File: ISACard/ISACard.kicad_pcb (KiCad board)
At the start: 2 copper layers, 171.5 x 95.9 mm, 96 parts, among them J1 Bus_ISA_8bit, J2 ICSP, J3 EXTSPI, J4 SERCON, J5 Conn_01x16, Q1 2N3904, SW1 SW_Push, U1 74LS86, U10 28C256, U11 ATmega328P-P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

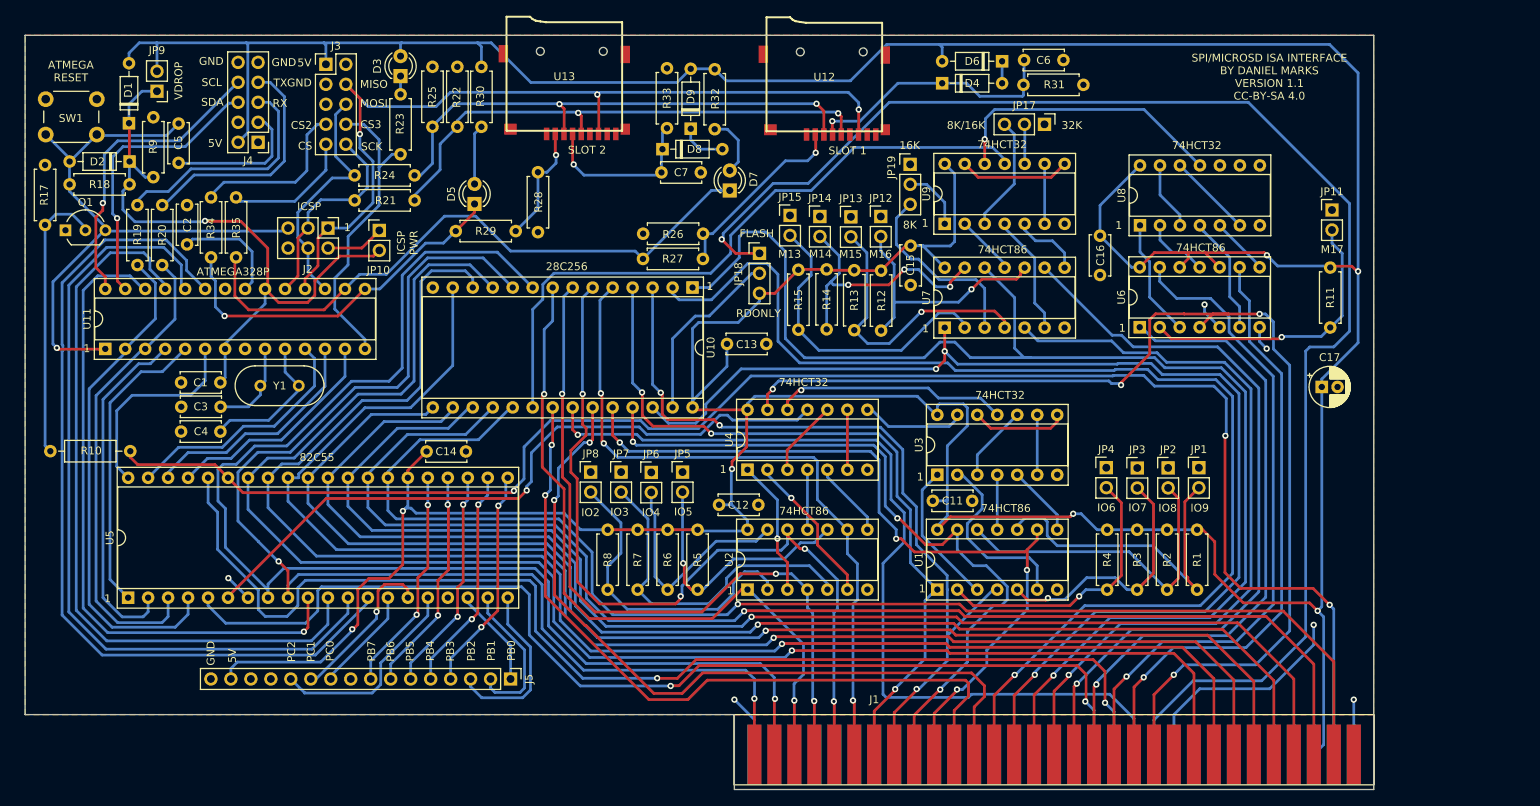
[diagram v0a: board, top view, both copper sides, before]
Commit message: moved SD card slots to edge
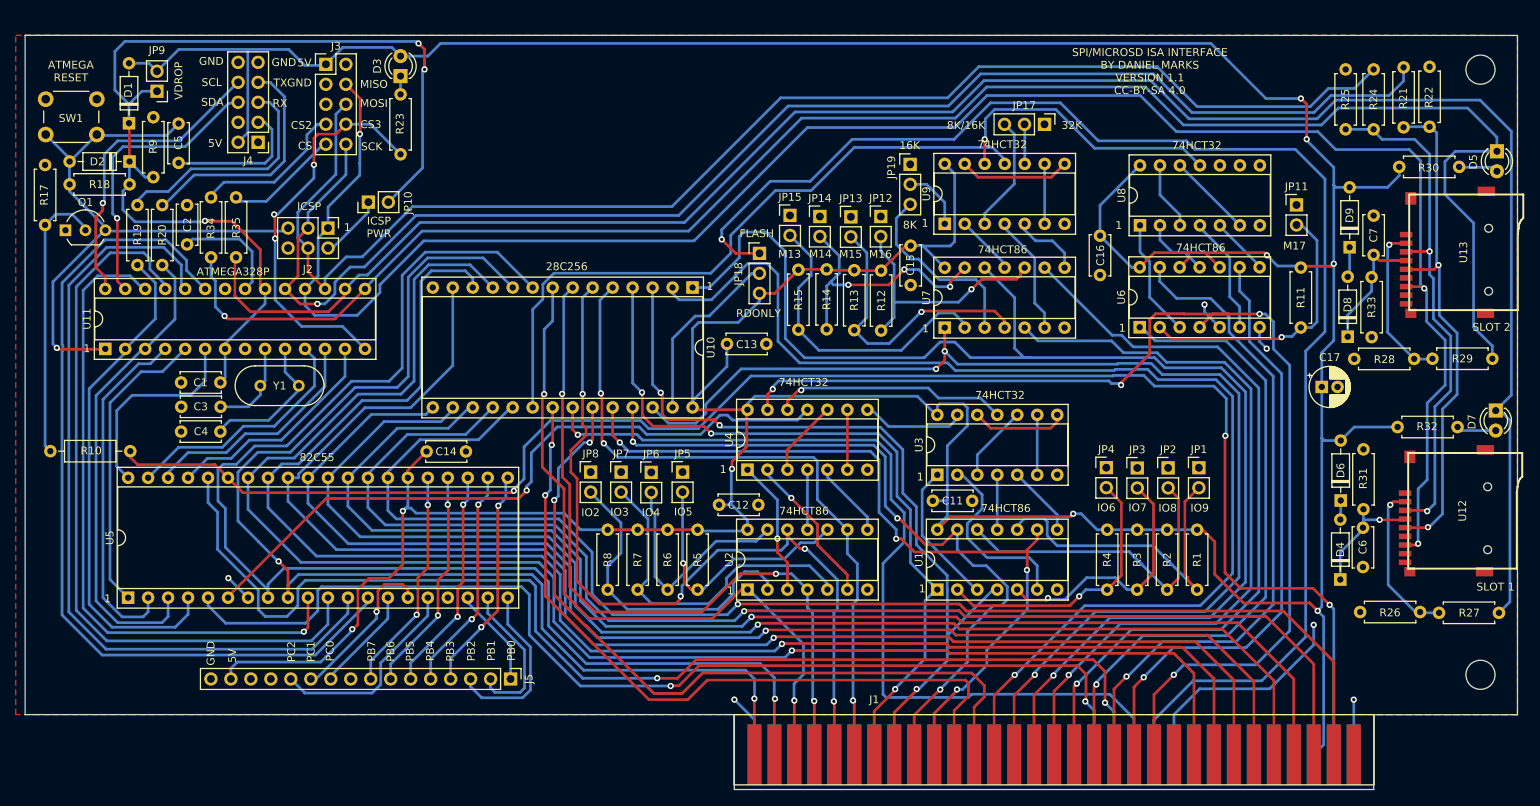
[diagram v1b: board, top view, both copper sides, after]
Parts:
- added H1: MountingHole, MountingHole:MountingHole_3.7mm, F.Cu at (236.0, 66.0)
- added H2: MountingHole, MountingHole:MountingHole_3.7mm, F.Cu at (236.0, 142.9)
- moved R21 134.4 mm to (226.2, 65.7), turned to -90 degrees
- moved R24 130.2 mm to (222.4, 66.0), turned to -90 degrees
- moved D5 130.1 mm to (238.1, 76.4), turned to -90 degrees
- moved R30 124.4 mm to (233.3, 78.4), turned to 180 degrees
- moved R22 123.6 mm to (229.5, 73.3)
- moved R29 117.7 mm to (229.9, 102.8), turned to 0 degrees
- moved R25 116.1 mm to (218.9, 73.6)
- moved R28 113.9 mm to (227.6, 102.8), turned to 180 degrees
- moved U13 107.2 mm to (225.7, 89.2), turned to -90 degrees
- moved R27 103.8 mm to (230.7, 135.1), turned to 0 degrees
- moved R26 103.1 mm to (228.3, 134.9)
- moved D7 101.3 mm to (237.9, 109.3), turned to -90 degrees
- moved R32 98.0 mm to (225.5, 111.4), turned to 0 degrees
- moved R33 91.6 mm to (222.2, 92.4), turned to -90 degrees
- moved D8 90.3 mm to (219.1, 100.0), turned to 90 degrees
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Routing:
- net CS2: track 46.5 -> 223.3 mm
- net CS: track 79.2 -> 248.8 mm
- net SCK: track 26.5 -> 183.0 mm, vias 0 -> 1
- net MOSI: track 30.5 -> 177.3 mm
- net MISO: track 109.8 -> 245.2 mm
- net Net-(D1-K): track 81.0 -> 130.2 mm, vias 1 -> 3
- net Net-(D4-K): track 33.3 -> 15.5 mm
- net CS3: track 39.0 -> 50.3 mm, vias 0 -> 3
- net +5V: track 631.5 -> 622.8 mm, vias 7 -> 9
- net Net-(D8-K): track 21.8 -> 16.2 mm, vias 1 -> 0
- net Net-(U13-~{CS}): track 15.2 -> 20.6 mm
- net Net-(U12-~{CS}): track 24.4 -> 20.3 mm
- net MEMW: track 185.5 -> 181.5 mm
- net Net-(D7-A): track 7.87 -> 5.04 mm
- net Net-(D5-A): track 7.63 -> 5.03 mm
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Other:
- board size 171.5 x 95.9 mm -> 189.7 x 95.9 mm

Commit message: Moved ATMEGA328P so that trace length is shorter
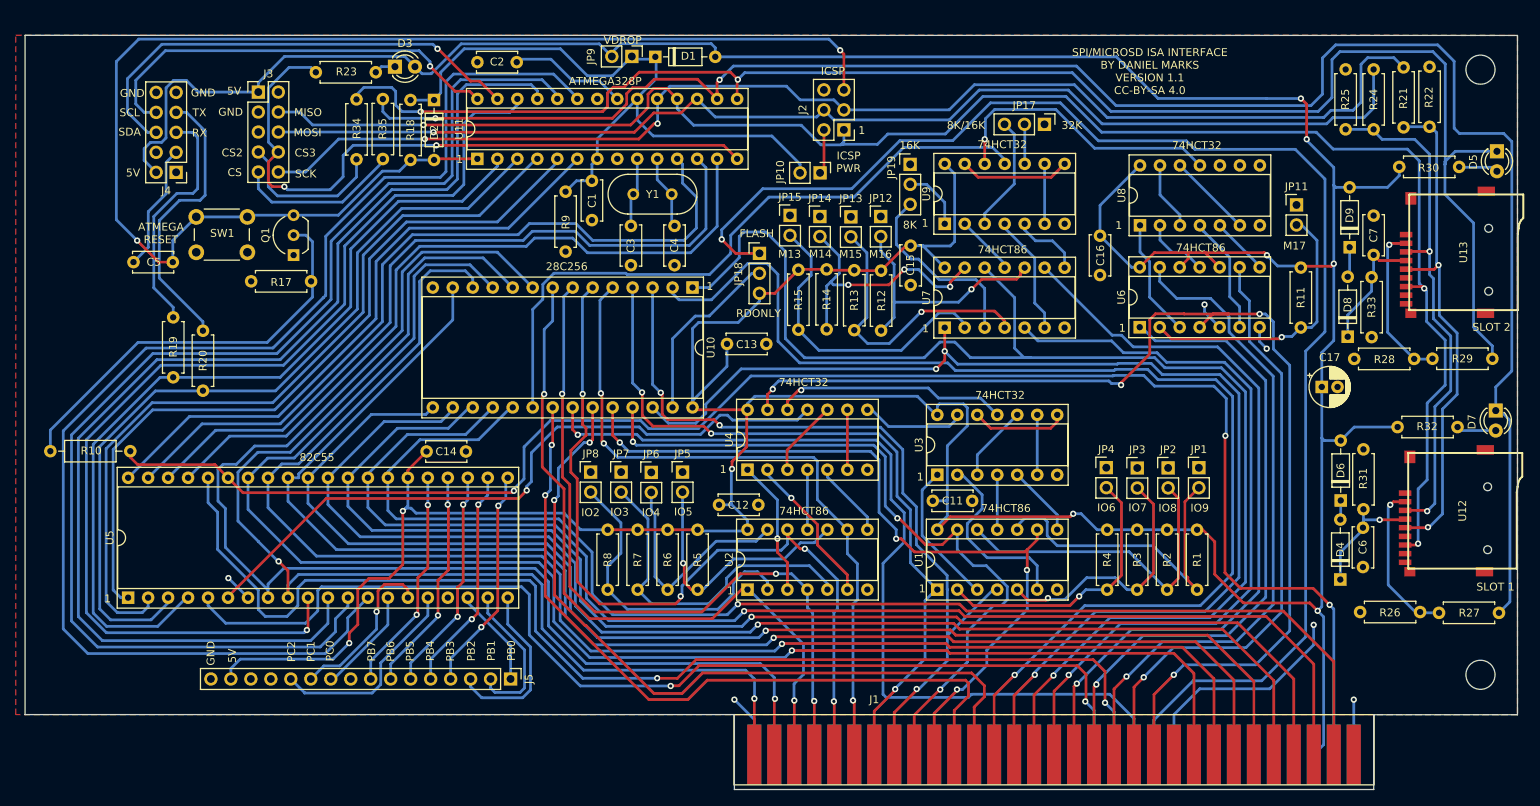
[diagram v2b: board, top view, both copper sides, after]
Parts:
- moved D1 67.4 mm to (131.1, 64.4), turned to 0 degrees
- moved J2 66.8 mm to (155.1, 73.7), turned to 180 degrees
- moved C4 66.2 mm to (133.5, 90.9), turned to 90 degrees
- moved JP9 60.5 mm to (128.1, 64.3), turned to -90 degrees
- moved JP10 57.5 mm to (152.0, 79.1), turned to -90 degrees
- moved C3 57.0 mm to (128.0, 85.9), turned to -90 degrees
- moved C1 53.7 mm to (123.0, 80.1), turned to -90 degrees
- moved Y1 53.3 mm to (133.2, 81.8)
- moved U11 53.1 mm to (108.5, 77.3)
- moved R9 52.4 mm to (119.7, 81.5), turned to -90 degrees
- moved C2 47.9 mm to (113.5, 65.0), turned to 180 degrees
- moved D2 39.5 mm to (103.0, 69.9), turned to -90 degrees
- moved R18 37.3 mm to (100.0, 69.9), turned to -90 degrees
- moved R17 34.6 mm to (87.3, 92.9), turned to 180 degrees
- moved Q1 29.2 mm to (85.1, 89.6), turned to 90 degrees
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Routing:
- net ARESET: track 79.0 -> 174.3 mm, vias 1 -> 2
- net PA5: track 31.2 -> 98.7 mm
- net PA6: track 29.9 -> 96.6 mm
- net PA7: track 28.8 -> 94.8 mm
- net PA3: track 38.1 -> 96.4 mm
- net PA2: track 44.6 -> 101.1 mm
- net PC4: track 110.5 -> 165.8 mm
- net PC6: track 95.1 -> 148.9 mm
- net PC7: track 83.7 -> 137.4 mm
- net PC5: track 103.3 -> 157.0 mm
- net PA4: track 26.0 -> 78.2 mm
- net PA1: track 60.7 -> 103.9 mm
- net PA0: track 64.1 -> 107.0 mm
- net Net-(D1-K): track 130.2 -> 88.0 mm, vias 3 -> 0
- net CS3: track 50.3 -> 85.0 mm, vias 3 -> 2
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
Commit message: minor pcb tweaks
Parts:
- moved D7 2.67 mm to (235.7, 107.9)
- moved D5 2.38 mm to (236.1, 75.1)
- moved R32 1.01 mm to (224.4, 111.3)
- moved R30 0.72 mm to (232.6, 78.4)
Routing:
- net CS2: track 204.2 -> 201.6 mm
- net +5V: track 623.7 -> 622.4 mm
- net Net-(D5-A): track 5.03 -> 3.88 mm
- net CS: track 232.8 -> 233.8 mm
- net Net-(U12-DI): track 65.7 -> 64.8 mm
- net Net-(D7-A): track 5.04 -> 4.42 mm

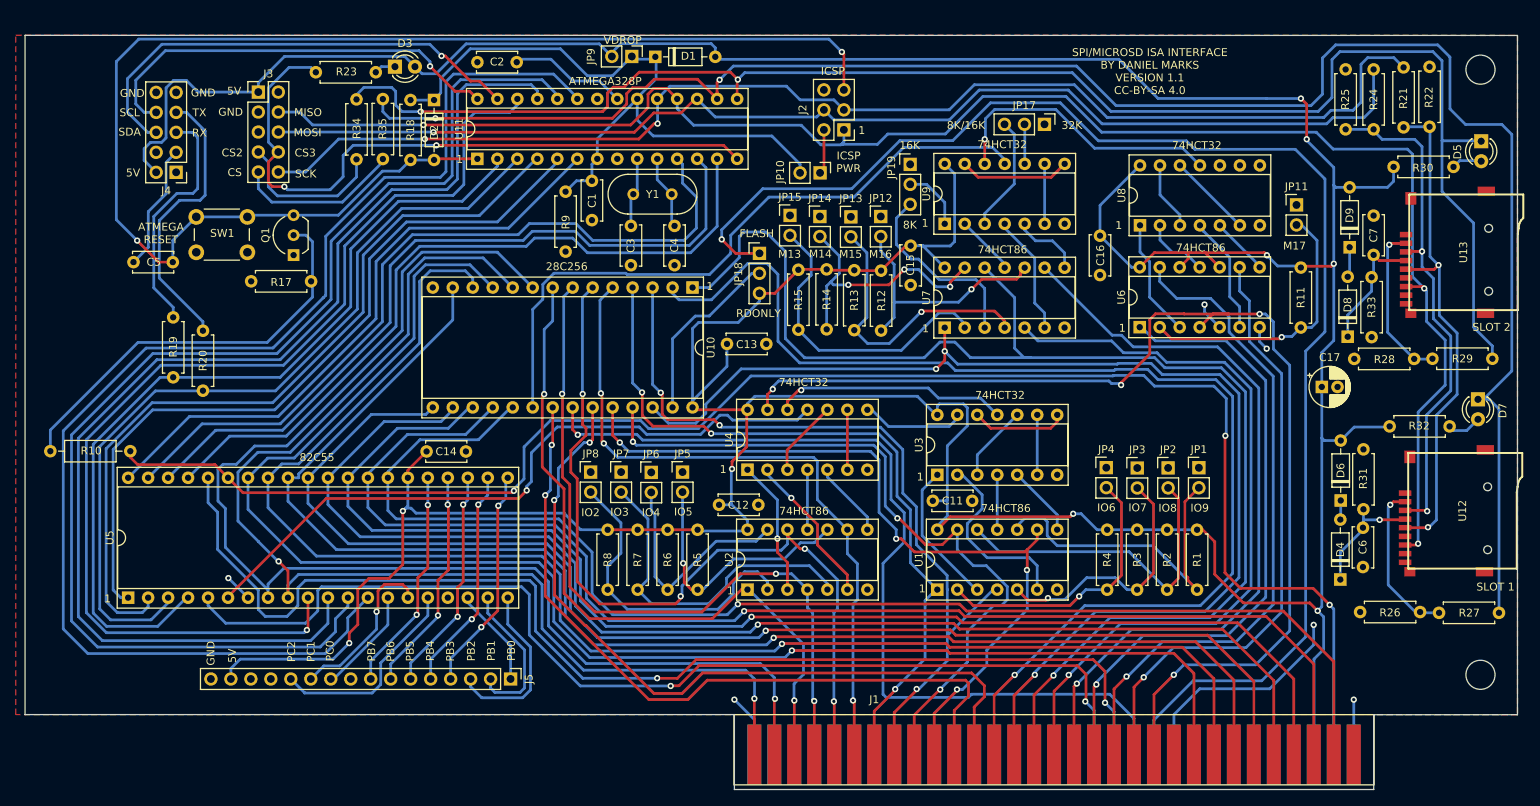
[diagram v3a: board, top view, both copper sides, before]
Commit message: Added IRQ connection to ethernet
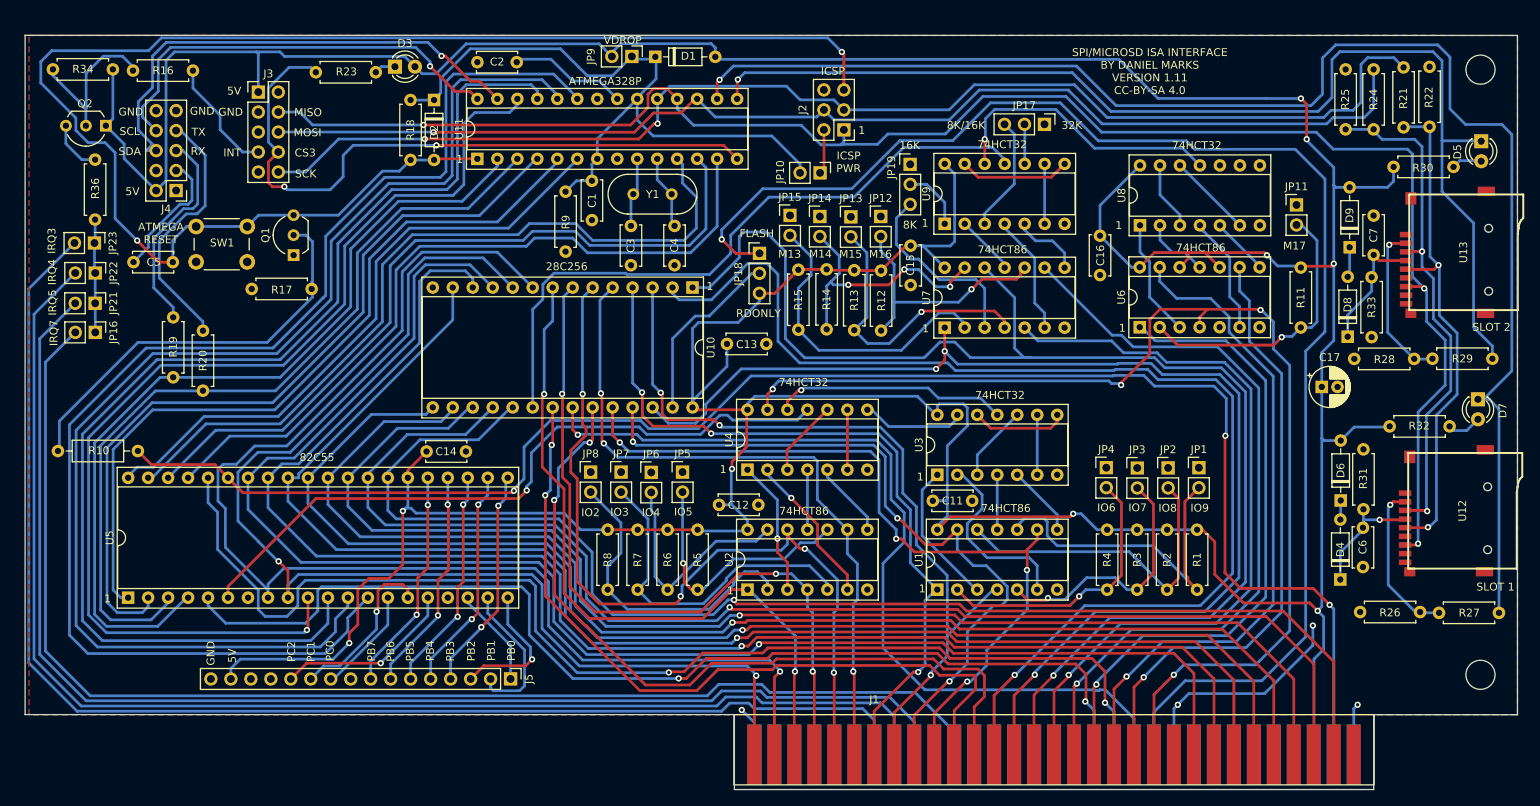
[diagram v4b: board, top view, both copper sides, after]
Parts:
- removed R35: 4k7, Resistor_THT:R_Axial_DIN0207_L6.3mm_D2.5mm_P7.62mm_Horizontal
- added JP16: JP, Connector_PinHeader_2.54mm:PinHeader_1x02_P2.54mm_Vertical, F.Cu at (59.9, 99.4)
- added JP21: JP, Connector_PinHeader_2.54mm:PinHeader_1x02_P2.54mm_Vertical, F.Cu at (59.9, 95.7)
- added JP22: JP, Connector_PinHeader_2.54mm:PinHeader_1x02_P2.54mm_Vertical, F.Cu at (59.9, 91.8)
- added JP23: JP, Connector_PinHeader_2.54mm:PinHeader_1x02_P2.54mm_Vertical, F.Cu at (59.8, 88.0)
- added Q2: 2N3906, Package_TO_SOT_THT:TO-92_Inline_Wide, F.Cu at (61.2, 73.1)
- added R16: 10k, Resistor_THT:R_Axial_DIN0207_L6.3mm_D2.5mm_P7.62mm_Horizontal, F.Cu at (72.3, 66.1)
- added R36: 1k, Resistor_THT:R_Axial_DIN0207_L6.3mm_D2.5mm_P7.62mm_Horizontal, F.Cu at (59.9, 77.4)
- R34: value 4k7 -> 100k
- moved R34 40.2 mm to (54.5, 66.0), turned to 0 degrees
- moved J4 2.32 mm to (70.2, 81.4)
- moved SW1 1.22 mm to (72.7, 85.9)
- moved R17 0.97 mm to (87.4, 93.9)
- moved R10 0.97 mm to (65.3, 114.5)
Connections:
- J1 pad 21: unconnected-(J1-IRQ7-Pad21) -> Net-(J1-IRQ7)
- J1 pad 23: unconnected-(J1-IRQ5-Pad23) -> Net-(J1-IRQ5)
- J1 pad 24: unconnected-(J1-IRQ4-Pad24) -> Net-(J1-IRQ4)
- J1 pad 25: unconnected-(J1-IRQ3-Pad25) -> Net-(J1-IRQ3)
- J3 pad 7: Net-(J3-Pin_7) -> INT
- J3 pad 9: Net-(J3-Pin_9) -> unconnected-(J3-Pin_9-Pad9)
- R34 pad 1: Net-(J3-Pin_7) -> Net-(Q2-B)
- R34 pad 2: CS2 -> +5V
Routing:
- net Net-(J1-IRQ3): track 0.00 -> 171.5 mm
- net Net-(J1-IRQ4): track 0.00 -> 169.4 mm
- net Net-(J1-IRQ5): track 0.00 -> 166.4 mm
- net Net-(J1-IRQ7): track 0.00 -> 166.0 mm
- net CS2: track 201.6 -> 146.4 mm, vias 2 -> 1
- net CS: track 233.8 -> 185.5 mm, vias 2 -> 1
- net +5V: track 622.4 -> 646.8 mm
- net Net-(Q2-B): track 0.00 -> 21.3 mm
- net Net-(J3-Pin_9): track 21.1 -> 0.00 mm
- net Net-(J3-Pin_7): track 19.9 -> 0.00 mm
- net INT: track 0.00 -> 15.0 mm
- net ARESET: track 174.3 -> 189.3 mm
- net Net-(JP16-A): track 0.00 -> 14.4 mm
- net GND: track 54.4 -> 42.2 mm, vias 6 -> 4
- net Net-(Q2-C): track 0.00 -> 6.84 mm
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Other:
- board text added: "INT"
- board text added: "IRQ3"
- board text added: "IRQ4"
- board text added: "IRQ5"
- board text added: "IRQ7"
- board text added: "SPI/MICROSD ISA INTERFACE BY DANIEL MARKS VERSION 1.11 CC-BY-SA 4.0"
- board text removed: "CS"
- board text removed: "CS2"
- board text removed: "SPI/MICROSD ISA INTERFACE BY DANIEL MARKS VERSION 1.1 CC-BY-SA 4.0"
